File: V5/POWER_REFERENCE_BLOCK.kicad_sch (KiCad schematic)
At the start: 28 parts, among them J201 3xAA_BATTERY, Q201 PMV48XP, SW201 MAIN_PWR_SW, U201 MCP3208-CI/P, U202 MCP6002-xP, U203 TPS7A2033PDBVR

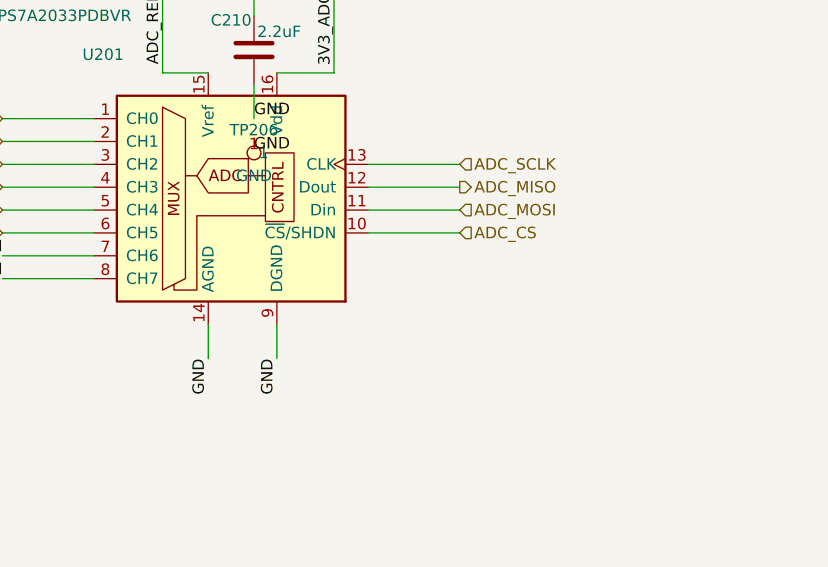
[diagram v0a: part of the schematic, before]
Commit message: add mcp3208 cs pullup
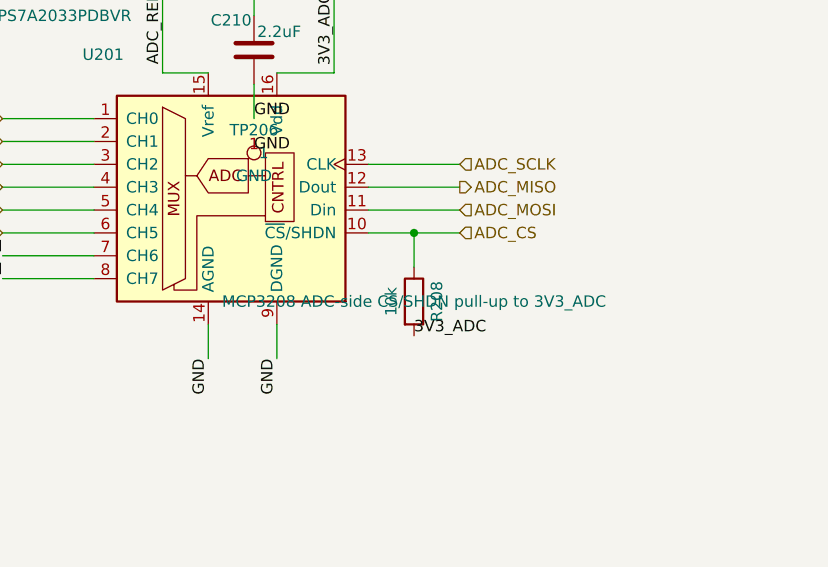
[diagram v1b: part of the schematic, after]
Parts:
- added R208: 10k, symbol Device:R
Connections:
- net 3V3_ADC: now also R208.2
- net ADC_CS: now also R208.1
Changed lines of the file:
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@@
 		(color 0 0 0 0)
 	)
+	(junction
+		(at 160.02 95.25)
+		(diameter 0)
+		(color 0 0 0 0)
+	)
 	(no_connect
 		(at 128.27 63.5)
@@
 	(wire
 		(pts
+			(xy 160.02 95.25) (xy 160.02 99.06)
+		)
+		(stroke
+			(width 0)
+			(type default)
+		)
+	)
+	(wire
+		(pts
 			(xy 154.94 92.71) (xy 165.1 92.71)
 		)
@@
 		)
 	)
+	(label "3V3_ADC"
+		(at 160.02 106.68 0)
+		(effects
+			(font
+				(size 1.27 1.27)
+			)
+			(justify left bottom)
+		)
+	)
 	(label "GND"
 		(at 254 127 0)
@@
 					(unit 1)
 				)
+			)
+		)
+	)
+	(symbol
+		(lib_id "Device:R")
+		(at 160.02 102.87 0)
+		(unit 1)
+		(body_style 1)
+		(exclude_from_sim no)
+		(in_bom yes)
+		(on_board yes)
+		(in_pos_files yes)
+		(dnp no)
+		(property "Reference" "R208"
+			(at 162.56 102.87 90)
+			(show_name no)
+			(do_not_autoplace no)
+			(effects
+				(font
+					(size 1.27 1.27)
+				)
+			)
+		)
+		(property "Value" "10k"
+			(at 157.48 102.87 90)
+			(show_name no)
+			(do_not_autoplace no)
+			(effects
+				(font
+					(size 1.27 1.27)
+				)
+			)
+		)
+		(property "Footprint" ""
+			(at 160.02 102.87 0)
+			(show_name no)
+			(do_not_autoplace no)
+			(effects
+				(font
+					(size 1.27 1.27)
+				)
+			)
+		)
+		(property "Datasheet" "~"
+			(at 160.02 102.87 0)
+			(hide yes)
+			(show_name no)
+			(do_not_autoplace no)
+			(effects
+				(font
+					(size 1.27 1.27)
+				)
+			)
+		)
+		(property "Description" "MCP3208 ADC-side CS/SHDN pull-up to 3V3_ADC"
+			(at 160.02 102.87 0)
+			(show_name no)
+			(do_not_autoplace no)
+			(effects
+				(font
+					(size 1.27 1.27)
+				)
+			)
+		)
+		(pin "1"
+		)
+		(pin "2"
+		)
+		(instances
+			(project "EMG_v5"
+				(path "/2c477672-822a-487d-bb83-204f5f41dbd8/4b7d3b9f-6eb5-4b2b-a72d-ec3d44a09101"
+					(reference "R208")
+					(unit 1)
+				)

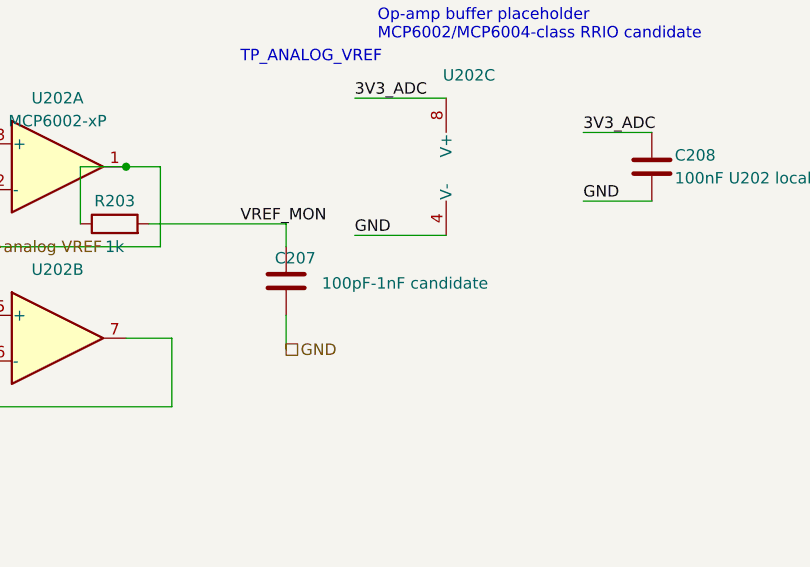
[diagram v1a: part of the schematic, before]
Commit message: finalize vref monitor capacitor at 220pf
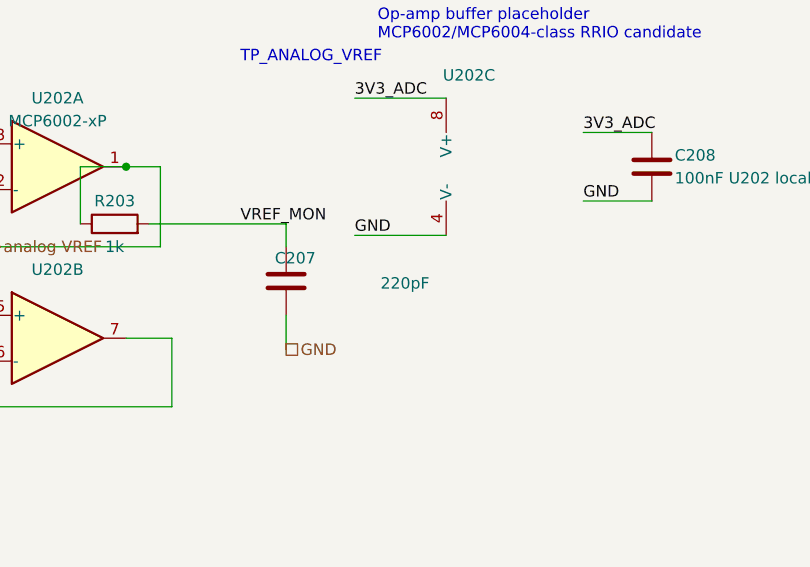
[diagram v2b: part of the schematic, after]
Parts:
- C207: value 100pF-1nF candidate -> 220pF
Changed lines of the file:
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@@
 			)
 		)
-		(property "Value" "100pF-1nF candidate"
+		(property "Value" "220pF"
 			(at 114.808 184.404 0)
 			(show_name no)

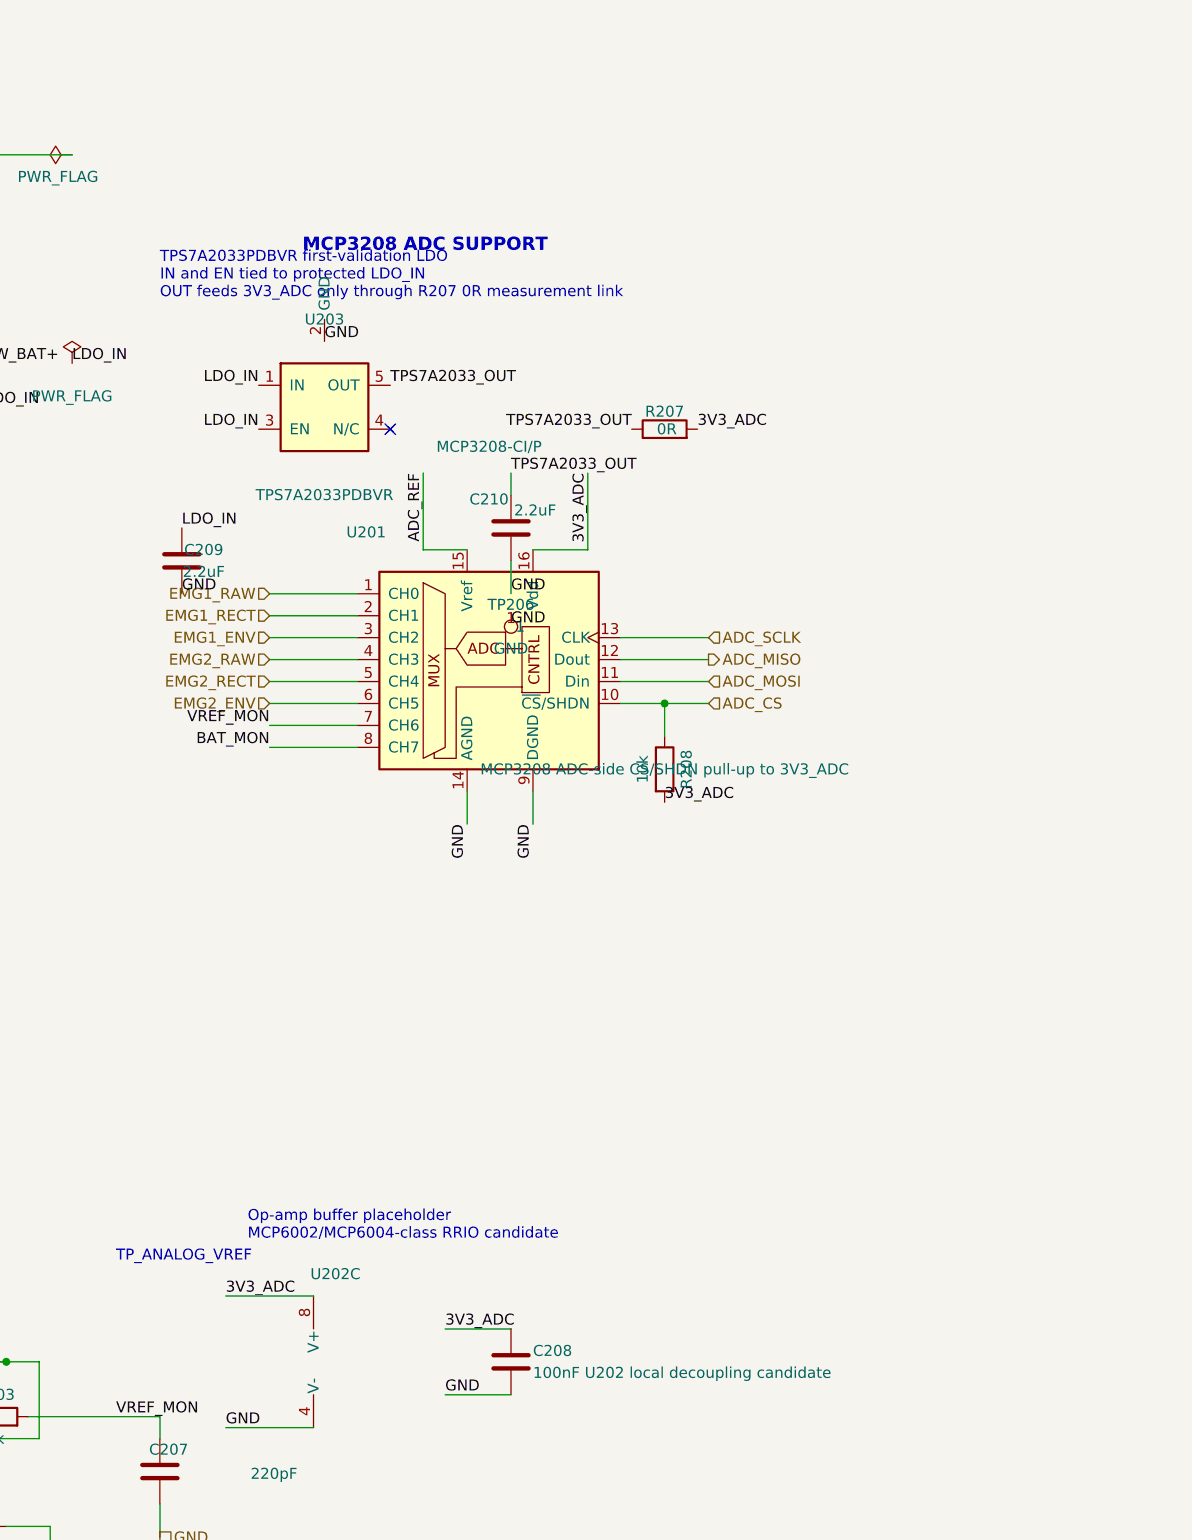
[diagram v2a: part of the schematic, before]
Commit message: finalize u202 local decoupling capacitor
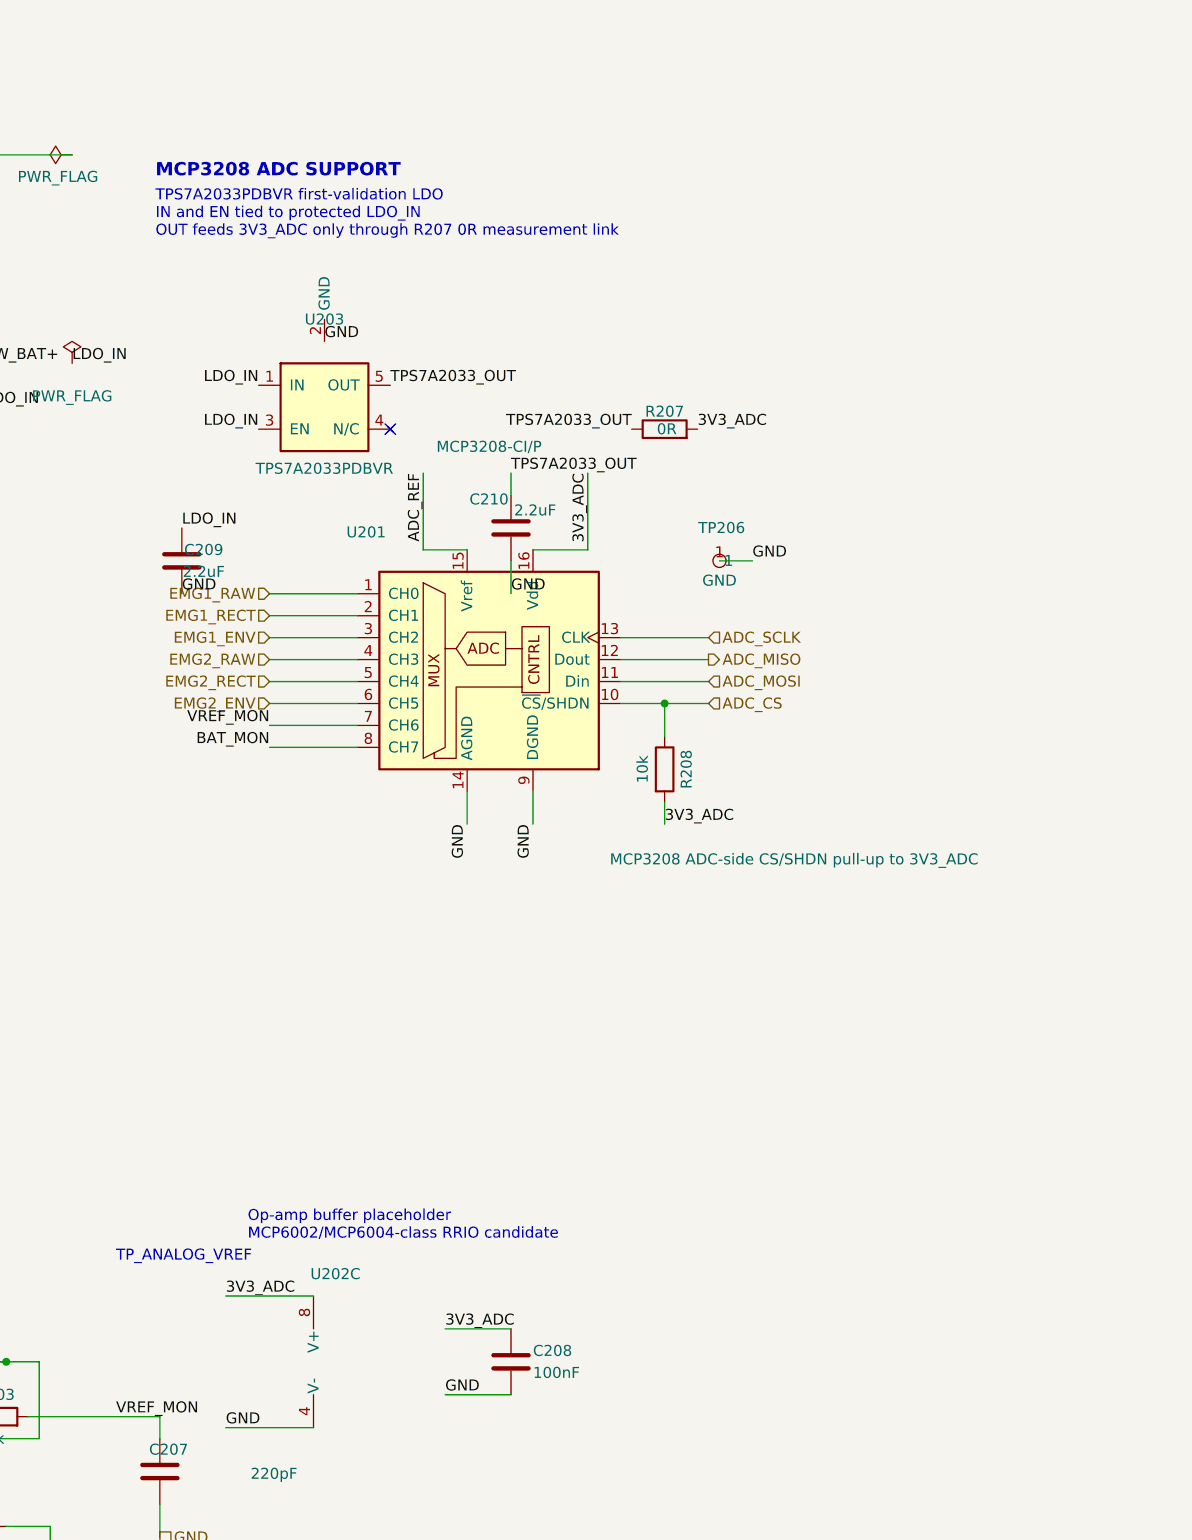
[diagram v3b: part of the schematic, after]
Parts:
- C208: value 100nF U202 local decoupling candidate -> 100nF
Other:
- moved on the sheet: TP206

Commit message: finalize adc reference network values
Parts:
- C205: value 100nF ADC_REF candidate -> 100nF
- C206: value 1uF ADC_REF optional -> 1uF
- R206: value 0R/10R candidate -> 0R
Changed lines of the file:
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@@
 			)
 		)
-		(property "Value" "100nF ADC_REF candidate"
+		(property "Value" "100nF"
 			(at 279.654 49.276 0)
 			(show_name no)
@@
 			)
 		)
-		(property "Value" "1uF ADC_REF optional"
+		(property "Value" "1uF"
 			(at 315.976 49.784 0)
 			(show_name no)
@@
 			)
 		)
-		(property "Value" "0R/10R candidate"
+		(property "Value" "0R"
 			(at 258.826 70.358 90)
 			(show_name no)

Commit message: finalize 3v3 adc rail decoupling values
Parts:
- C203: value 100nF VDD candidate -> 100nF
- C204: value 1uF or 4.7uF bulk candidate -> 1uF
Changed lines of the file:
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@@
 			)
 		)
-		(property "Value" "100nF VDD candidate"
+		(property "Value" "100nF"
 			(at 277.622 34.29 0)
 			(show_name no)
@@
 			)
 		)
-		(property "Value" "1uF or 4.7uF bulk candidate"
+		(property "Value" "1uF"
 			(at 319.024 34.29 0)
 			(show_name no)

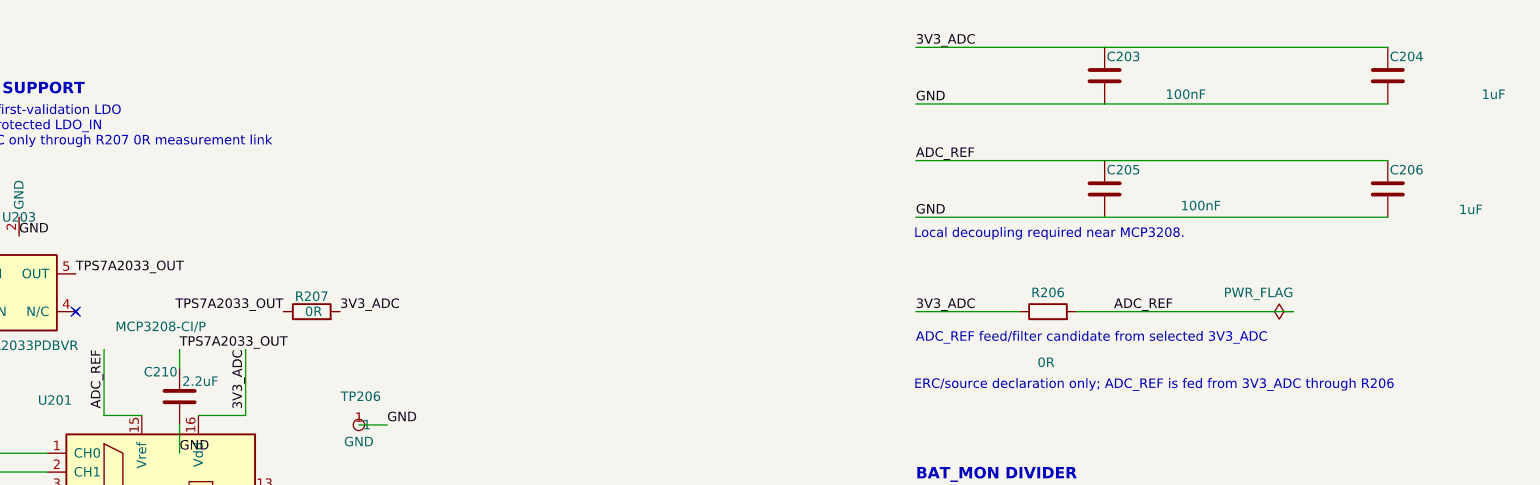
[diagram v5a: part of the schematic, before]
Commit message: add battery powered carrier supply path
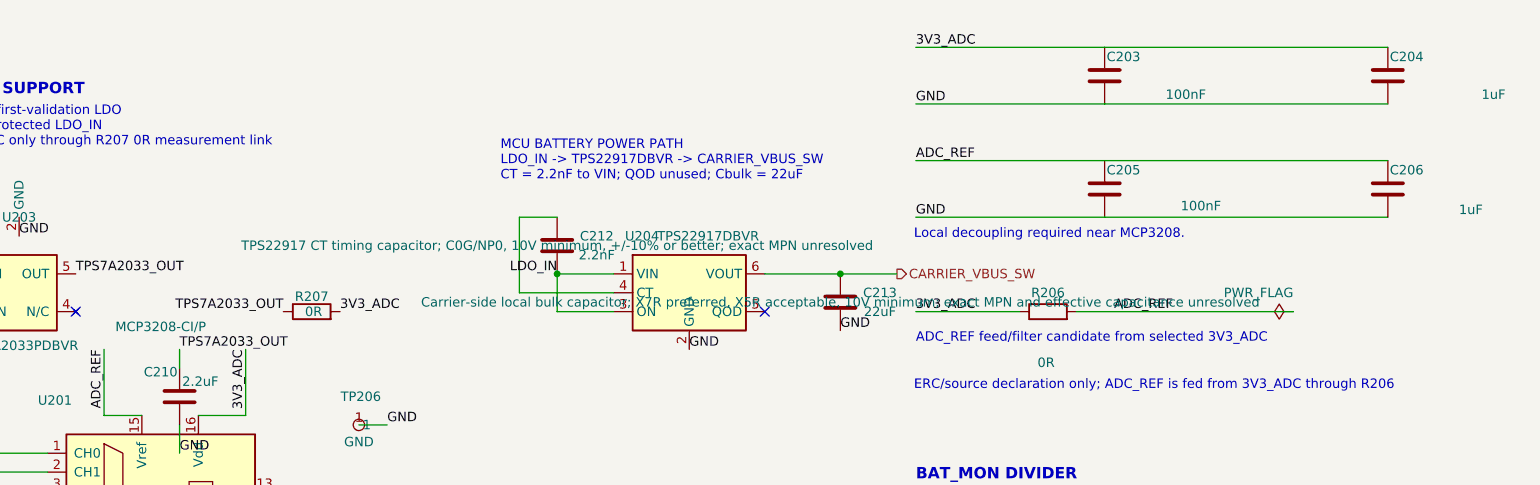
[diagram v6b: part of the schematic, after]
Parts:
- added C212: 2.2nF, symbol Device:C
- added C213: 22uF, symbol Device:C
- added U204: TPS22917DBVR, Package_TO_SOT_SMD:SOT-23-6, symbol Power_Management:TPS22917DBV
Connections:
- net GND: now also C213.2, U204.2 (GND)
- net LDO_IN: now also C212.2, U204.1 (VIN), U204.3 (ON)
- new net: C212.1, U204.4 (CT)
- new net CARRIER_VBUS_SW: C213.1, U204.6 (VOUT)
- no-connect marks 1 -> 2
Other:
- note added: "MCU BATTERY POWER PATH LDO_IN -> TPS22917DBVR -> CARRIER_VBUS_SW CT = 2.2nF to VIN; QOD unused; Cbulk = 22uF"
